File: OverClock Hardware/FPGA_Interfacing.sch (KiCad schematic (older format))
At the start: 16 parts, among them J2 JTAG_HDR, U3 10M02SCE144

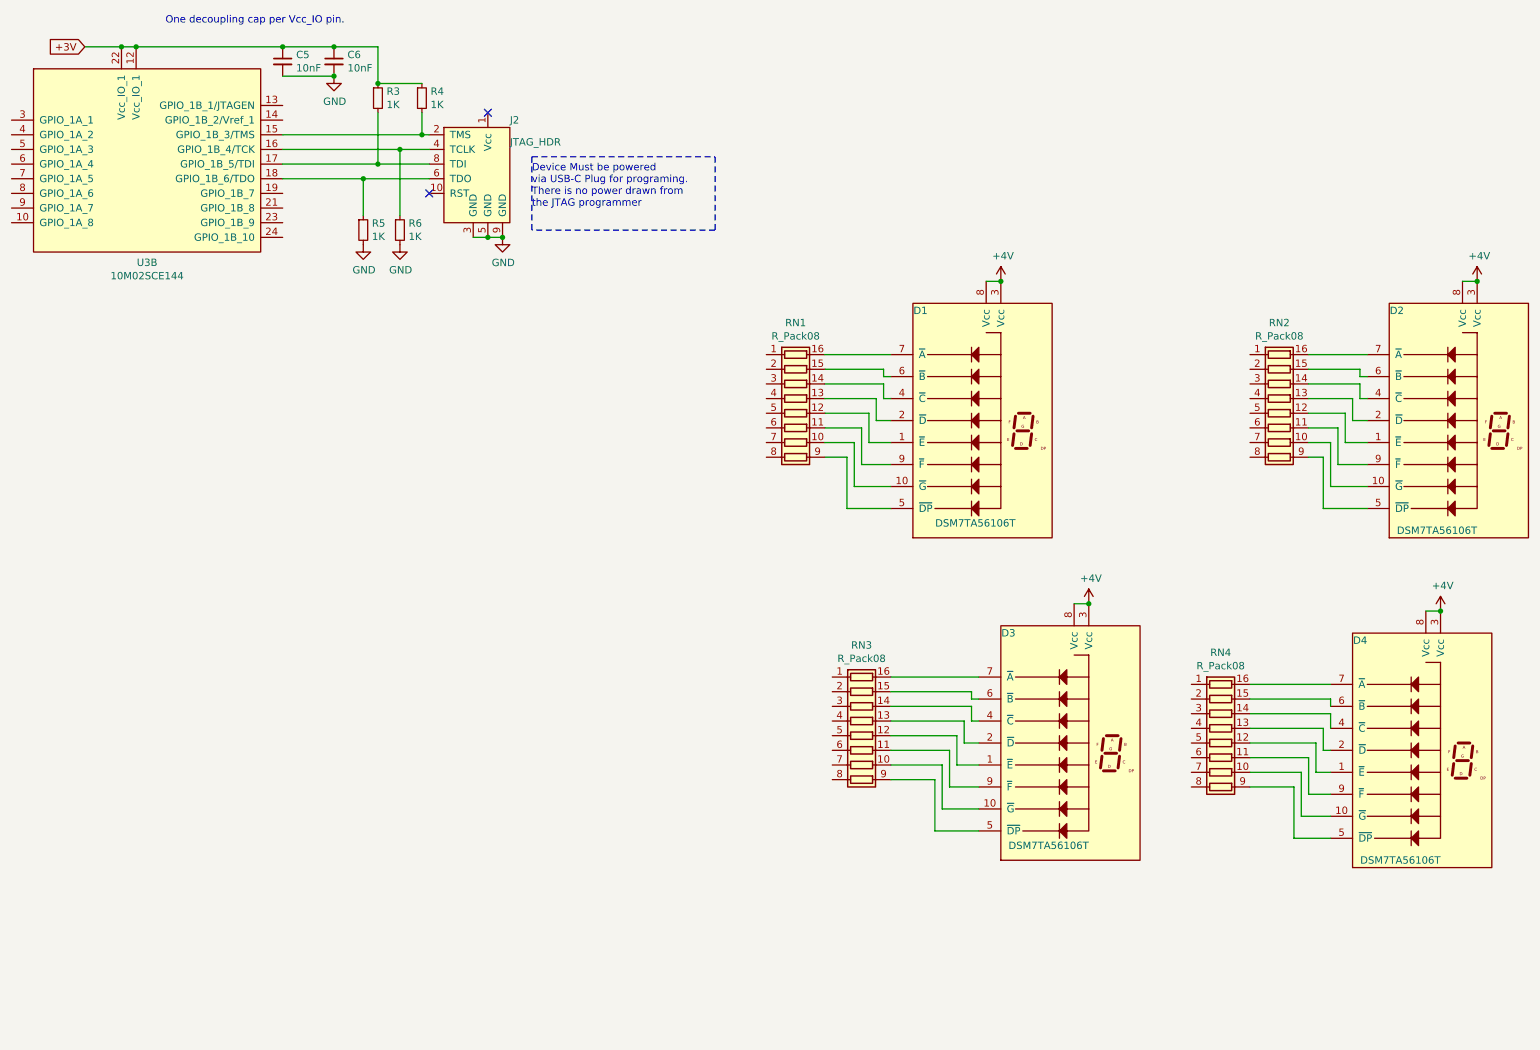
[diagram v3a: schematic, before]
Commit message: Interfaced Hours Digits to FPGA
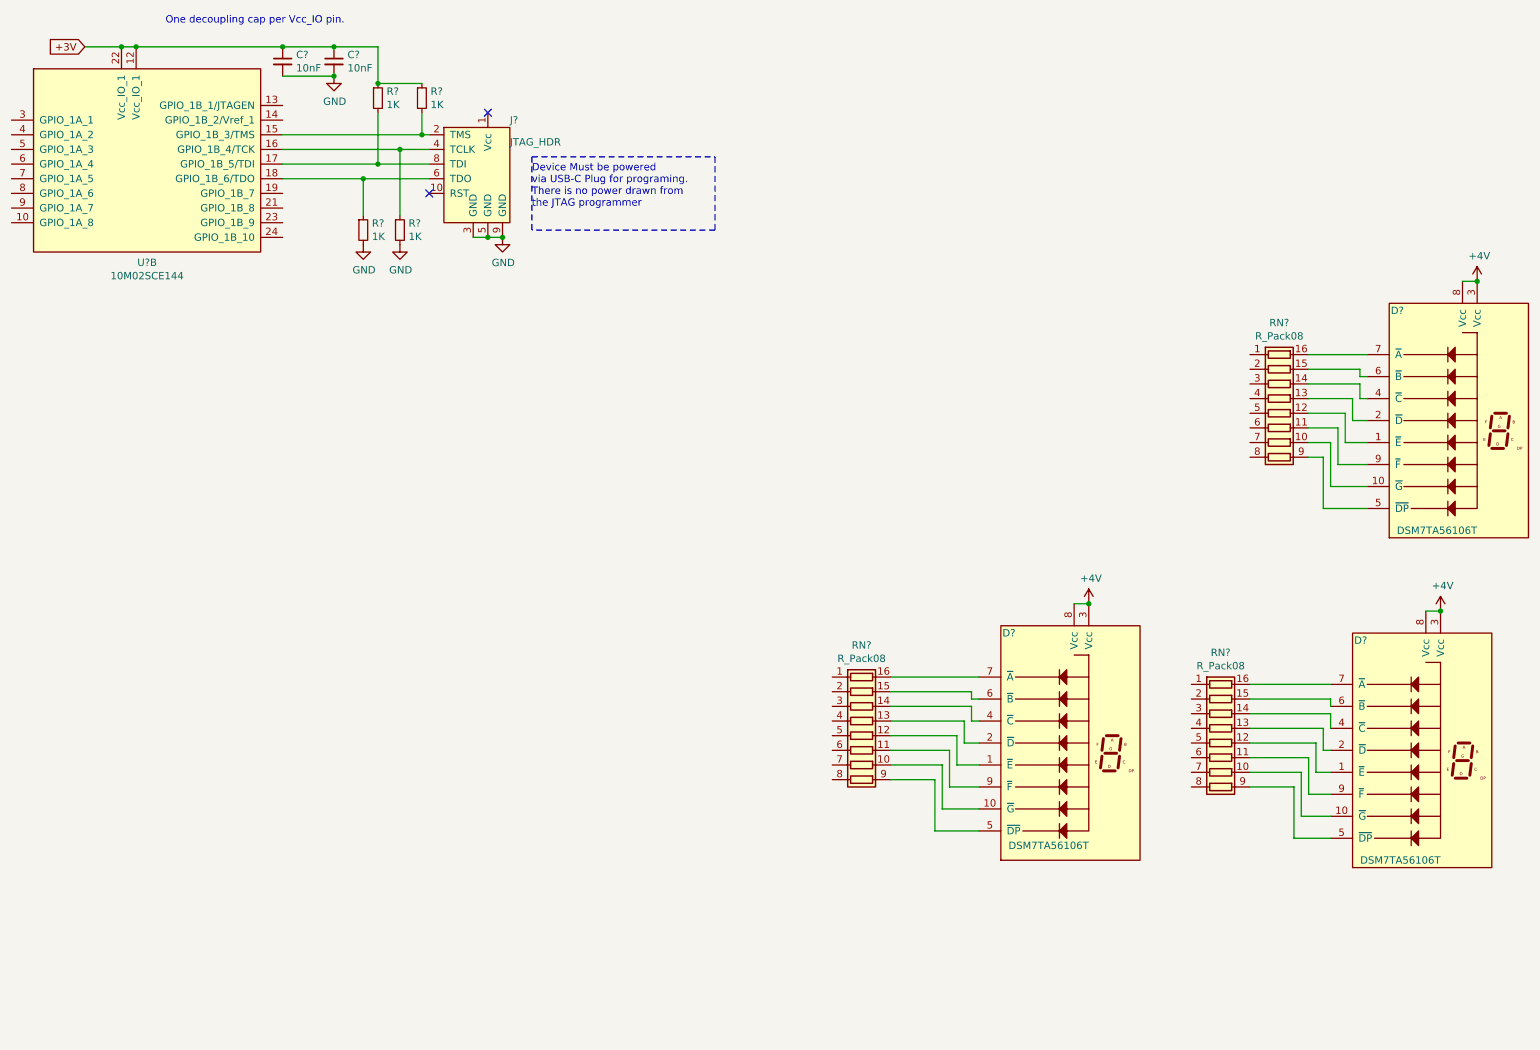
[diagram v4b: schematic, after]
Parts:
- removed D1: DSM7TA56106T, symbol Maxted_Libs:DSM7TA56106T
- removed RN1: R_Pack08, Maxted Libs:1506_Array, symbol Device:R_Pack08
- renumbered C5 to C?, C6 to C?, D2 to D?, D3 to D?, D4 to D?, J2 to J?, R5 to R?, R6 to R?, R3 to R?, R4 to R?, RN3 to RN?, RN2 to RN?, RN4 to RN?, U3 to U?
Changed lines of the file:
@@
 $Descr A4 11693 8268
 encoding utf-8
-Sheet 3 3
+Sheet 3 4
 Title ""
 Date ""
@@
 $Comp
 L Maxted_Libs:DSM7TA56106T D?
-U 1 1 5C66BBD1
-P 7250 3350
-AR Path="/5C66BBD1" Ref="D?"  Part="1"
-AR Path="/5C66B7E8/5C66BBD1" Ref="D1"  Part="1"
-F 0 "D1" H 6850 4150 50  0000 R CNN
-F 1 "DSM7TA56106T" H 7450 2700 50  0000 R CNN
-F 2 "" H 7550 3350 50  0001 C CNN
-F 3 "" H 7550 3350 50  0001 C CNN
-	1    7250 3350
-	1    0    0    -1
-$EndComp
-$Comp
-L Maxted_Libs:DSM7TA56106T D?
 U 1 1 5C66BBD8
 P 10500 3350
 AR Path="/5C66BBD8" Ref="D?"  Part="1"
-AR Path="/5C66B7E8/5C66BBD8" Ref="D2"  Part="1"
-F 0 "D2" H 10100 4150 50  0000 R CNN
+AR Path="/5C66B7E8/5C66BBD8" Ref="D?"  Part="1"
+F 0 "D?" H 10100 4150 50  0000 R CNN
 F 1 "DSM7TA56106T" H 10600 2650 50  0000 R CNN
 F 2 "" H 10800 3350 50  0001 C CNN
@@
 P 7850 5550
 AR Path="/5C66BBDF" Ref="D?"  Part="1"
-AR Path="/5C66B7E8/5C66BBDF" Ref="D3"  Part="1"
-F 0 "D3" H 7450 6350 50  0000 R CNN
+AR Path="/5C66B7E8/5C66BBDF" Ref="D?"  Part="1"
+F 0 "D?" H 7450 6350 50  0000 R CNN
 F 1 "DSM7TA56106T" H 7950 4900 50  0000 R CNN
 F 2 "" H 8150 5550 50  0001 C CNN
@@
 P 10250 5600
 AR Path="/5C66BBE6" Ref="D?"  Part="1"
-AR Path="/5C66B7E8/5C66BBE6" Ref="D4"  Part="1"
-F 0 "D4" H 9850 6400 50  0000 R CNN
+AR Path="/5C66B7E8/5C66BBE6" Ref="D?"  Part="1"
+F 0 "D?" H 9850 6400 50  0000 R CNN
 F 1 "DSM7TA56106T" H 10350 4900 50  0000 R CNN
 F 2 "" H 10550 5600 50  0001 C CNN
@@
 	7850 4550 7950 4550
 Wire Wire Line
-	7250 2350 7350 2350
-Wire Wire Line
 	10500 2350 10600 2350
 Wire Wire Line
 	10250 4600 10350 4600
-$Comp
-L Device:R_Pack08 RN?
-U 1 1 5C66BBF2
-P 5950 3250
-AR Path="/5C66BBF2" Ref="RN?"  Part="1"
-AR Path="/5C66B7E8/5C66BBF2" Ref="RN1"  Part="1"
-F 0 "RN1" V 5333 3250 50  0000 C CNN
-F 1 "R_Pack08" V 5424 3250 50  0000 C CNN
-F 2 "Maxted Libs:1506_Array" V 6425 3250 50  0001 C CNN
-F 3 "~" H 5950 3250 50  0001 C CNN
-F 4 "https://www.digikey.co.nz/product-detail/en/panasonic-electronic-components/EXB-2HV181JV/Y1181CT-ND/285372" V 5950 3250 50  0001 C CNN "Vendor"
-	1    5950 3250
-	0    1    1    0
-$EndComp
-Wire Wire Line
-	6150 2850 6600 2850
-Wire Wire Line
-	6600 3000 6550 3000
-Wire Wire Line
-	6550 3000 6550 2950
-Wire Wire Line
-	6550 2950 6150 2950
-Wire Wire Line
-	6150 3050 6550 3050
-Wire Wire Line
-	6550 3050 6550 3150
-Wire Wire Line
-	6550 3150 6600 3150
-Wire Wire Line
-	6600 3300 6500 3300
-Wire Wire Line
-	6500 3300 6500 3150
-Wire Wire Line
-	6500 3150 6150 3150
-Wire Wire Line
-	6150 3250 6450 3250
-Wire Wire Line
-	6450 3250 6450 3450
-Wire Wire Line
-	6450 3450 6600 3450
-Wire Wire Line
-	6600 3600 6400 3600
-Wire Wire Line
-	6400 3600 6400 3350
-Wire Wire Line
-	6400 3350 6150 3350
-Wire Wire Line
-	6150 3450 6350 3450
-Wire Wire Line
-	6350 3450 6350 3750
-Wire Wire Line
-	6350 3750 6600 3750
-Wire Wire Line
-	6150 3550 6300 3550
-Wire Wire Line
-	6300 3550 6300 3900
-Wire Wire Line
-	6300 3900 6600 3900
 $Comp
 L Device:R_Pack08 RN?
@@
 P 6400 5450
 AR Path="/5C66BC10" Ref="RN?"  Part="1"
-AR Path="/5C66B7E8/5C66BC10" Ref="RN3"  Part="1"
-F 0 "RN3" V 5783 5450 50  0000 C CNN
+AR Path="/5C66B7E8/5C66BC10" Ref="RN?"  Part="1"
+F 0 "RN?" V 5783 5450 50  0000 C CNN
 F 1 "R_Pack08" V 5874 5450 50  0000 C CNN
 F 2 "Maxted Libs:1506_Array" V 6875 5450 50  0001 C CNN
@@
 P 9250 3250
 AR Path="/5C66BC18" Ref="RN?"  Part="1"
-AR Path="/5C66B7E8/5C66BC18" Ref="RN2"  Part="1"
-F 0 "RN2" V 8633 3250 50  0000 C CNN
+AR Path="/5C66B7E8/5C66BC18" Ref="RN?"  Part="1"
+F 0 "RN?" V 8633 3250 50  0000 C CNN
 F 1 "R_Pack08" V 8724 3250 50  0000 C CNN
 F 2 "Maxted Libs:1506_Array" V 9725 3250 50  0001 C CNN
@@
 P 8850 5500
 AR Path="/5C66BC20" Ref="RN?"  Part="1"
-AR Path="/5C66B7E8/5C66BC20" Ref="RN4"  Part="1"
-F 0 "RN4" V 8233 5500 50  0000 C CNN
+AR Path="/5C66B7E8/5C66BC20" Ref="RN?"  Part="1"
+F 0 "RN?" V 8233 5500 50  0000 C CNN
 F 1 "R_Pack08" V 8324 5500 50  0000 C CNN
 F 2 "Maxted Libs:1506_Array" V 9325 5500 50  0001 C CNN
@@
 $Comp
 L power:+4V #PWR?
-U 1 1 5C66BC67
-P 7350 2350
-AR Path="/5C66BC67" Ref="#PWR?"  Part="1"
-AR Path="/5C66B7E8/5C66BC67" Ref="#PWR06"  Part="1"
-F 0 "#PWR06" H 7350 2200 50  0001 C CNN
-F 1 "+4V" H 7365 2523 50  0000 C CNN
-F 2 "" H 7350 2350 50  0001 C CNN
-F 3 "" H 7350 2350 50  0001 C CNN
-	1    7350 2350
-	1    0    0    -1
-$EndComp
-Connection ~ 7350 2350
-$Comp
-L power:+4V #PWR?
 U 1 1 5C66BC6E
 P 10600 2350
 AR Path="/5C66BC6E" Ref="#PWR?"  Part="1"
-AR Path="/5C66B7E8/5C66BC6E" Ref="#PWR07"  Part="1"
-F 0 "#PWR07" H 10600 2200 50  0001 C CNN
+AR Path="/5C66B7E8/5C66BC6E" Ref="#PWR?"  Part="1"
+F 0 "#PWR?" H 10600 2200 50  0001 C CNN
 F 1 "+4V" H 10615 2523 50  0000 C CNN
 F 2 "" H 10600 2350 50  0001 C CNN
@@
 P 10350 4600
 AR Path="/5C66BC74" Ref="#PWR?"  Part="1"
-AR Path="/5C66B7E8/5C66BC74" Ref="#PWR09"  Part="1"
-F 0 "#PWR09" H 10350 4450 50  0001 C CNN
+AR Path="/5C66B7E8/5C66BC74" Ref="#PWR?"  Part="1"
+F 0 "#PWR?" H 10350 4450 50  0001 C CNN
 F 1 "+4V" H 10365 4773 50  0000 C CNN
 F 2 "" H 10350 4600 50  0001 C CNN
@@
 P 7950 4550
 AR Path="/5C66BC7A" Ref="#PWR?"  Part="1"
-AR Path="/5C66B7E8/5C66BC7A" Ref="#PWR08"  Part="1"
-F 0 "#PWR08" H 7950 4400 50  0001 C CNN
+AR Path="/5C66B7E8/5C66BC7A" Ref="#PWR?"  Part="1"
+F 0 "#PWR?" H 7950 4400 50  0001 C CNN
 F 1 "+4V" H 7965 4723 50  0000 C CNN
 F 2 "" H 7950 4550 50  0001 C CNN
@@
 Connection ~ 10600 2350
 $Comp
-L Maxted_Libs:10M02SCE144 U3
+L Maxted_Libs:10M02SCE144 U?
 U 2 1 5C67791D
 P 1450 1600
-F 0 "U3" H 1525 978 50  0000 C CNN
+F 0 "U?" H 1525 978 50  0000 C CNN
 F 1 "10M02SCE144" H 1525 887 50  0000 C CNN
 F 2 "Maxted Libs:QFP-144_EPAD_20x20_Pitch0.5mm" H 2450 2400 50  0001 C CNN
@@
 +3V
 $Comp
-L Device:R_Small R5
+L Device:R_Small R?
 U 1 1 5C68AD28
 P 3000 2000
-F 0 "R5" H 3059 2046 50  0000 L CNN
+F 0 "R?" H 3059 2046 50  0000 L CNN
 F 1 "1K" H 3059 1955 50  0000 L CNN
 F 2 "" H 3000 2000 50  0001 C CNN
@@
 $EndComp
 $Comp
-L power:GND #PWR012
+L power:GND #PWR?
 U 1 1 5C68ADAE
 P 3000 2100
-F 0 "#PWR012" H 3000 1850 50  0001 C CNN
+F 0 "#PWR?" H 3000 1850 50  0001 C CNN
 F 1 "GND" H 3005 1927 50  0000 C CNN
 F 2 "" H 3000 2100 50  0001 C CNN
@@
 	3250 1450 3250 1900
 $Comp
-L Device:R_Small R6
+L Device:R_Small R?
 U 1 1 5C692EE8
 P 3250 2000
-F 0 "R6" H 3309 2046 50  0000 L CNN
+F 0 "R?" H 3309 2046 50  0000 L CNN
 F 1 "1K" H 3309 1955 50  0000 L CNN
 F 2 "" H 3250 2000 50  0001 C CNN
@@
 $EndComp
 $Comp
-L power:GND #PWR013
+L power:GND #PWR?
 U 1 1 5C692FE7
 P 3250 2100
-F 0 "#PWR013" H 3250 1850 50  0001 C CNN
+F 0 "#PWR?" H 3250 1850 50  0001 C CNN
 F 1 "GND" H 3255 1927 50  0000 C CNN
 F 2 "" H 3250 2100 50  0001 C CNN
@@
 	3100 1550 3100 1200
 $Comp
-L Device:R_Small R3
+L Device:R_Small R?
 U 1 1 5C69923E
 P 3100 1100
-F 0 "R3" H 3159 1146 50  0000 L CNN
+F 0 "R?" H 3159 1146 50  0000 L CNN
 F 1 "1K" H 3159 1055 50  0000 L CNN
 F 2 "" H 3100 1100 50  0001 C CNN
@@
 $EndComp
 $Comp
-L Device:R_Small R4
+L Device:R_Small R?
 U 1 1 5C699292
 P 3400 1100
-F 0 "R4" H 3459 1146 50  0000 L CNN
+F 0 "R?" H 3459 1146 50  0000 L CNN
 F 1 "1K" H 3459 1055 50  0000 L CNN
 F 2 "" H 3400 1100 50  0001 C CNN
@@
 Connection ~ 3100 1000
 $Comp
-L Maxted_Libs:JTAG_HDR J2
+L Maxted_Libs:JTAG_HDR J?
 U 1 1 5C6A069B
 P 3800 1600
-F 0 "J2" H 4000 1950 50  0000 L CNN
+F 0 "J?" H 4000 1950 50  0000 L CNN
 F 1 "JTAG_HDR" H 4000 1800 50  0000 L CNN
 F 2 "Connector_PinHeader_2.54mm:PinHeader_2x05_P2.54mm_Vertical" H 3650 2500 50  0001 C CNN
@@
 $EndComp
 $Comp
-L power:GND #PWR011
+L power:GND #PWR?
 U 1 1 5C6A0707
 P 3950 2050
-F 0 "#PWR011" H 3950 1800 50  0001 C CNN
+F 0 "#PWR?" H 3950 1800 50  0001 C CNN
 F 1 "GND" H 3955 1877 50  0000 C CNN
 F 2 "" H 3950 2050 50  0001 C CNN
@@
 	4150 2000 4150 1500
 $Comp
-L Device:C_Small C5
+L Device:C_Small C?
 U 1 1 5C6B33C4
 P 2450 850
-F 0 "C5" H 2542 896 50  0000 L CNN
+F 0 "C?" H 2542 896 50  0000 L CNN
 F 1 "10nF" H 2542 805 50  0000 L CNN
 F 2 "" H 2450 850 50  0001 C CNN
@@
 $EndComp
 $Comp
-L power:GND #PWR010
+L power:GND #PWR?
 U 1 1 5C6B34AA
 P 2800 950
-F 0 "#PWR010" H 2800 700 50  0001 C CNN
+F 0 "#PWR?" H 2800 700 50  0001 C CNN
 F 1 "GND" H 2805 777 50  0000 C CNN
 F 2 "" H 2800 950 50  0001 C CNN
@@
 	2450 1450 3250 1450
 $Comp
-L Device:C_Small C6
+L Device:C_Small C?
 U 1 1 5C6CAB44
 P 2800 850
-F 0 "C6" H 2892 896 50  0000 L CNN
+F 0 "C?" H 2892 896 50  0000 L CNN
 F 1 "10nF" H 2892 805 50  0000 L CNN
 F 2 "" H 2800 850 50  0001 C CNN

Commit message: Interfaced minutes digits to FPGA and added time selection methods
Interfaced the two 7 Segment displays used for displaying the minutes to the FPGA. 

Added 4 Tactile switches to increment/decrement the hours and minutes separately.

Added a header to allow for setting of the time via UART.
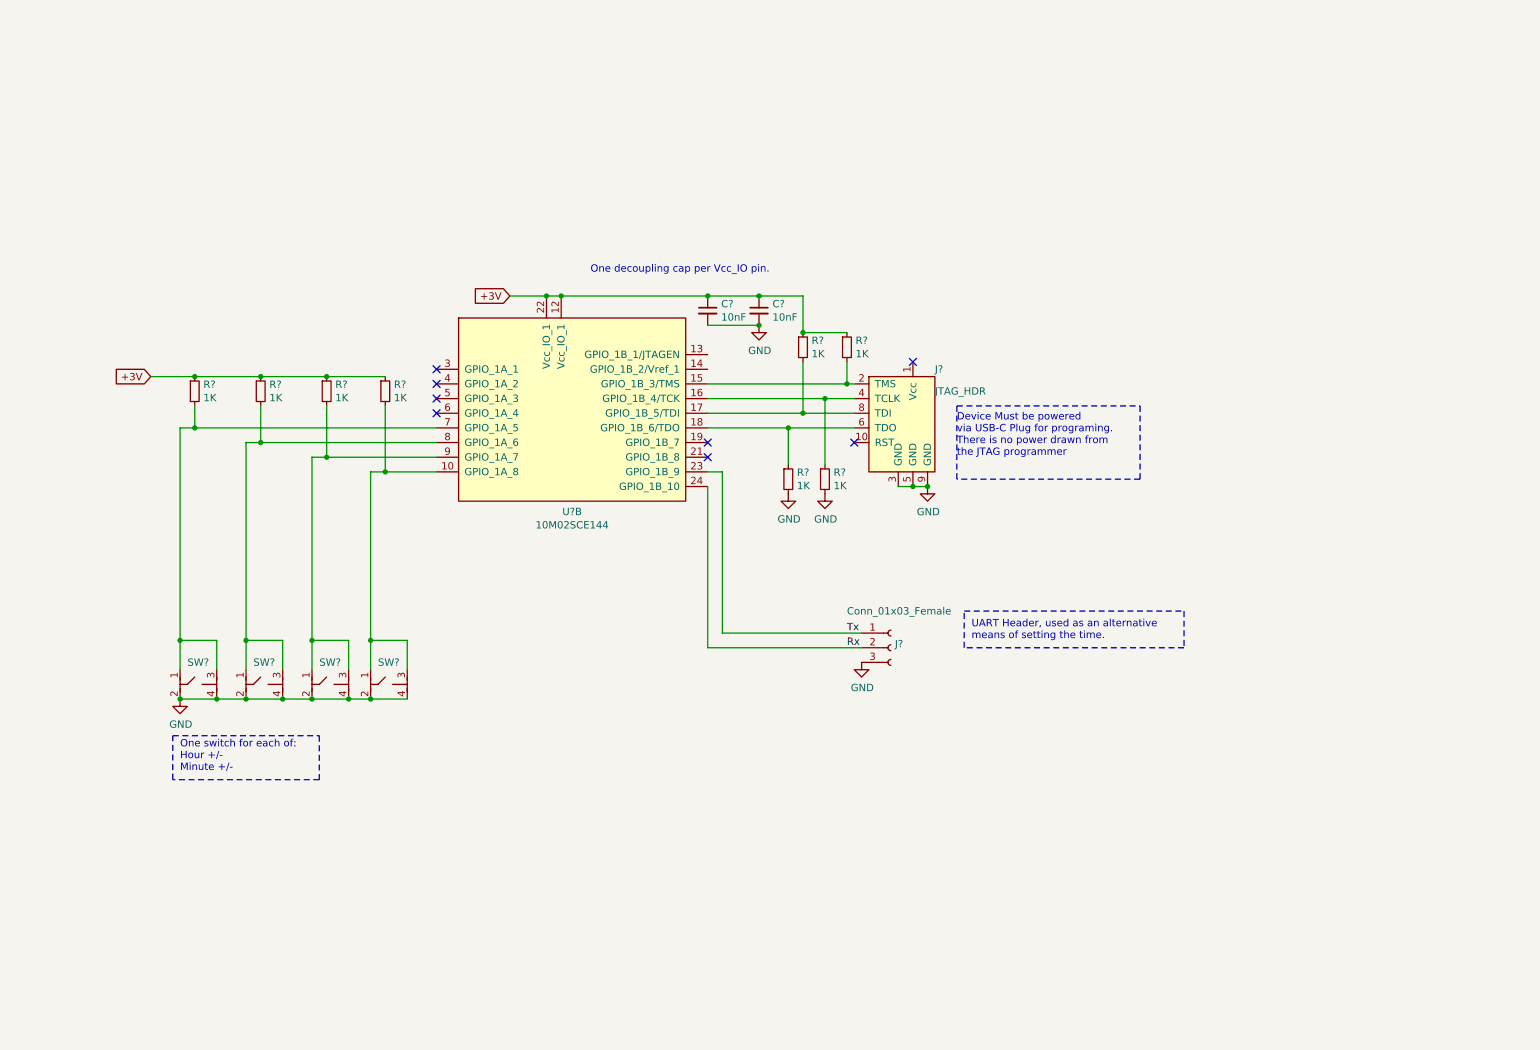
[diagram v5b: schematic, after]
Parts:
- removed D? (x3): DSM7TA56106T, symbol Maxted_Libs:DSM7TA56106T
- removed RN? (x3): R_Pack08, Maxted Libs:1506_Array, symbol Device:R_Pack08
- added J?: Conn_01x03_Female, Connector_Harwin:Harwin_M20-89003xx_1x03_P2.54mm_Horizontal, symbol Connector:Conn_01x03_Female
- added R? (x4): 1K, Resistor_SMD:R_0805_2012Metric_Pad1.15x1.40mm_HandSolder, symbol Device:R_Small
- added SW? (x4): Switch_Momentary, Maxted Libs:Switch_Momentary, symbol Maxted_Libs:Switch_Momentary
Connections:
- net +3V: now also R?.1, R?.1, R?.1, R?.1
- net GND: now also J?.3 (Pin_3), SW?.2, SW?.2, SW?.2, SW?.2, SW?.4, SW?.4, SW?.4, SW?.4
- net at U?.10 (GPIO_1A_8): now also R?.2, SW?.1, SW?.3
- net Tx: now reaches U?.23 (GPIO_1B_9)
- net Tx: now also J?.1 (Pin_1)
- net Rx: now reaches U?.24 (GPIO_1B_10)
- net Rx: now also J?.2 (Pin_2)
- net at U?.7 (GPIO_1A_5): now also R?.2, SW?.1, SW?.3
- net at U?.8 (GPIO_1A_6): now also R?.2, SW?.1, SW?.3
- net at U?.9 (GPIO_1A_7): now also R?.2, SW?.1, SW?.3
- no-connect marks 2 -> 8
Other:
- note added: "One switch for each of:\nHour +/-\nMinute +/-"
- note added: "UART Header, used as an alternative \nmeans of setting the time."
- moved on the sheet: C?, J?, R?, U?B
